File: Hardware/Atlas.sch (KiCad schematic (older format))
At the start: 46 parts, among them J1 DC, U1 MS5611, U2 HTU21D, U3 uSD Card, U4 RFD900, U5 MPU9150, U6 XBEE, U7 VENUS838LPX-L, U8 AOZ1031

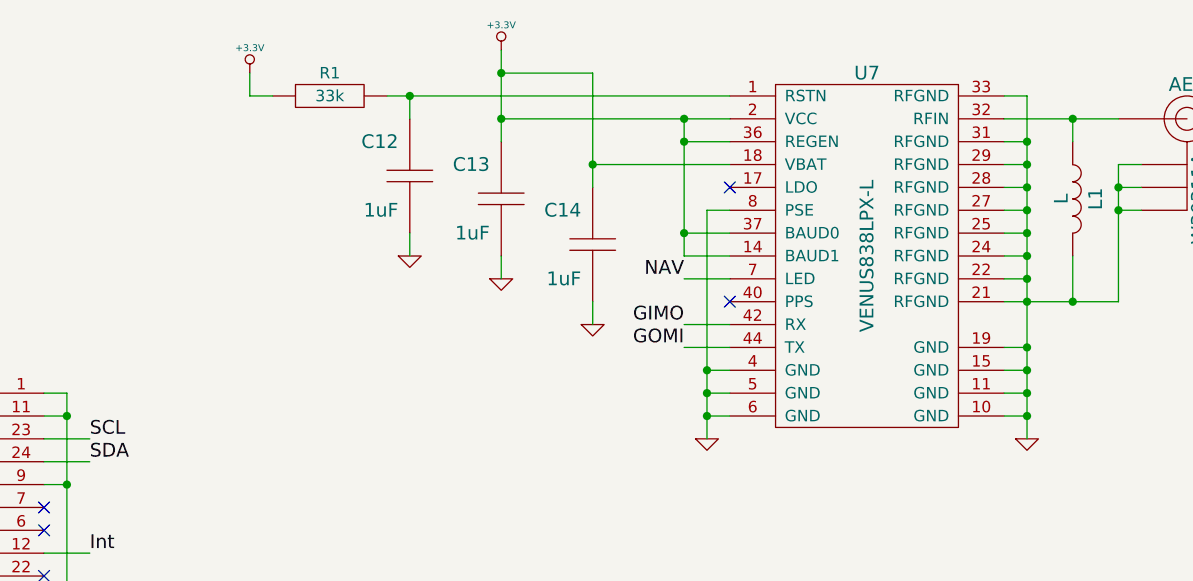
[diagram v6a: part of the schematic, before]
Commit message: Update GPS to support Flash and ROM versions
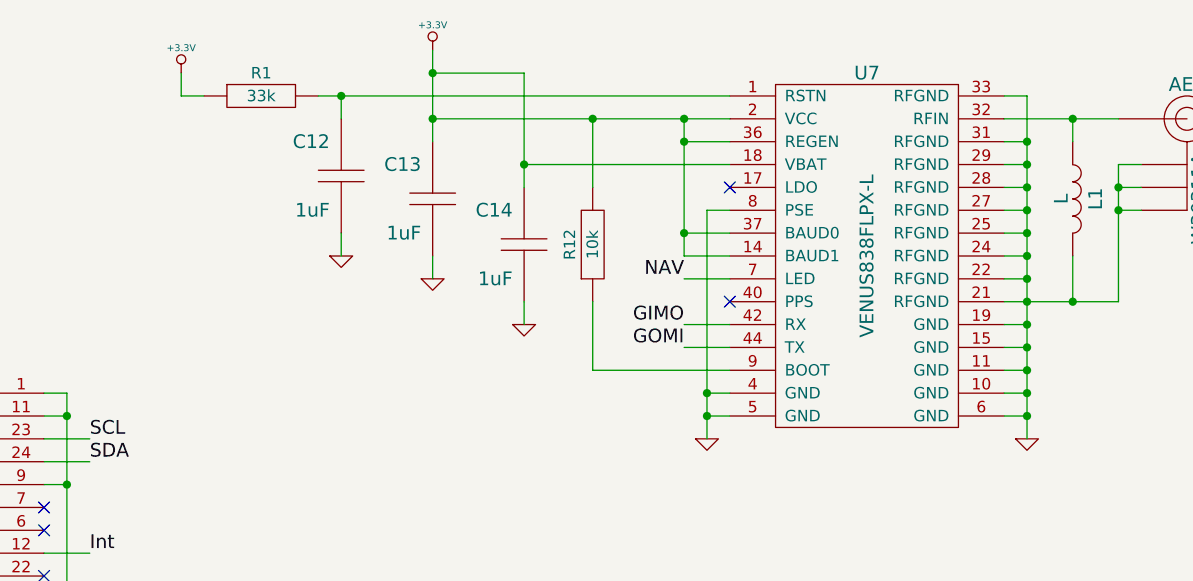
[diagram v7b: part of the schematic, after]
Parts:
- removed U7: VENUS838LPX-L, symbol VENUS838LPX-L
- added R12: 10k, RESC1608-N, symbol R
- added U7: VENUS838FLPX-L, ~, symbol VENUS838FLPX-L
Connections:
- net +3.3V: now also R12.2, U7.14 (BAUD1), U7.18 (VBAT), U7.2 (VCC), U7.36 (REGEN), U7.37 (BAUD0)
- net GIMO: now also U7.42 (RX)
- net GND: now also U7.10 (GND), U7.11 (GND), U7.15 (GND), U7.19 (GND), U7.21 (RFGND), U7.22 (RFGND), U7.24 (RFGND), U7.25 (RFGND), U7.27 (RFGND), U7.28 (RFGND), U7.29 (RFGND), U7.31 (RFGND), U7.33 (RFGND), U7.4 (GND), U7.5 (GND), U7.6 (GND), U7.8 (PSE)
- net GOMI: now also U7.44 (TX)
- net NAV: now also U7.7 (LED)
- net at C12.1, R1.2: now also U7.1 (RSTN)
- net at AE1.P, L1.2: now also U7.32 (RFIN)
- new net: R12.1, U7.9 (BOOT)
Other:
- moved on the sheet: C12, C13, C14, R1
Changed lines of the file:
@@
 Sheet 1 1
 Title "Atlas (Nucleo Shield)"
-Date "26 may 2014"
+Date "1 jun 2014"
 Rev "1"
 Comp "Aerodyne Labs"
@@
 L R R1
 U 1 1 537F99E2
-P 7050 1100
-F 0 "R1" H 7050 1200 50  0000 C CNN
-F 1 "33k" H 7050 1100 50  0000 C CNN
-F 2 "~" H 7050 1100 60  0000 C CNN
-F 3 "~" H 7050 1100 60  0000 C CNN
-F 4 "W" H 7050 1000 50  0001 C CNN "Power"
-F 5 "%" H 7050 900 50  0001 C CNN "Tolerance"
-	1    7050 1100
+P 6750 1100
+F 0 "R1" H 6750 1200 50  0000 C CNN
+F 1 "33k" H 6750 1100 50  0000 C CNN
+F 2 "~" H 6750 1100 60  0000 C CNN
+F 3 "~" H 6750 1100 60  0000 C CNN
+F 4 "W" H 6750 1000 50  0001 C CNN "Power"
+F 5 "%" H 6750 900 50  0001 C CNN "Tolerance"
+	1    6750 1100
 	1    0    0    -1
 $EndComp
@@
 L C C12
 U 1 1 537F99FD
-P 7400 1450
-F 0 "C12" H 7450 1600 60  0000 L CNN
-F 1 "1uF" H 7450 1300 60  0000 L CNN
-F 2 "CAPC1608-N" H 7400 1450 60  0001 C CNN
-F 3 "~" H 7400 1450 60  0000 C CNN
-F 4 "Samsung" H 7400 1450 60  0001 C CNN "MFR Name"
-F 5 "CL10B105KP8NNNC" H 7400 1450 60  0001 C CNN "MFR Part No"
-F 6 "1276-1946-1-ND" H 7400 1450 60  0001 C CNN "Distributor Part No"
-F 7 "10V" H 7350 1300 60  0001 R CNN "Voltage"
-F 8 "X7R" H 7350 1600 60  0001 R CNN "Dielectric"
-	1    7400 1450
+P 7100 1450
+F 0 "C12" H 7150 1600 60  0000 L CNN
+F 1 "1uF" H 7150 1300 60  0000 L CNN
+F 2 "CAPC1608-N" H 7100 1450 60  0001 C CNN
+F 3 "~" H 7100 1450 60  0000 C CNN
+F 4 "Samsung" H 7100 1450 60  0001 C CNN "MFR Name"
+F 5 "CL10B105KP8NNNC" H 7100 1450 60  0001 C CNN "MFR Part No"
+F 6 "1276-1946-1-ND" H 7100 1450 60  0001 C CNN "Distributor Part No"
+F 7 "10V" H 7050 1300 60  0001 R CNN "Voltage"
+F 8 "X7R" H 7050 1600 60  0001 R CNN "Dielectric"
+	1    7100 1450
 	-1   0    0    -1
 $EndComp
@@
 L +3.3V #PWR017
 U 1 1 537F9A2D
-P 6700 1000
-F 0 "#PWR017" H 6700 960 30  0001 C CNN
-F 1 "+3.3V" H 6700 1110 30  0000 C CNN
-F 2 "" H 6700 1000 60  0000 C CNN
-F 3 "" H 6700 1000 60  0000 C CNN
-	1    6700 1000
-	1    0    0    -1
-$EndComp
-$Comp
-L VENUS838LPX-L U7
-U 1 1 537FB717
-P 9400 1800
-F 0 "U7" H 9400 2600 60  0000 C CNN
-F 1 "VENUS838LPX-L" V 9400 1800 60  0000 C CNN
-F 2 "" H 9400 1800 60  0000 C CNN
-F 3 "" H 9400 1800 60  0000 C CNN
-	1    9400 1800
+P 6400 1000
+F 0 "#PWR017" H 6400 960 30  0001 C CNN
+F 1 "+3.3V" H 6400 1110 30  0000 C CNN
+F 2 "" H 6400 1000 60  0000 C CNN
+F 3 "" H 6400 1000 60  0000 C CNN
+	1    6400 1000
 	1    0    0    -1
 $EndComp
@@
 L +3.3V #PWR018
 U 1 1 537FB7C0
-P 7800 900
-F 0 "#PWR018" H 7800 860 30  0001 C CNN
-F 1 "+3.3V" H 7800 1010 30  0000 C CNN
-F 2 "" H 7800 900 60  0000 C CNN
-F 3 "" H 7800 900 60  0000 C CNN
-	1    7800 900
+P 7500 900
+F 0 "#PWR018" H 7500 860 30  0001 C CNN
+F 1 "+3.3V" H 7500 1010 30  0000 C CNN
+F 2 "" H 7500 900 60  0000 C CNN
+F 3 "" H 7500 900 60  0000 C CNN
+	1    7500 900
 	1    0    0    -1
 $EndComp
@@
 L GND #PWR020
 U 1 1 537FBC7D
-P 8200 2100
-F 0 "#PWR020" H 8200 2100 30  0001 C CNN
-F 1 "GND" H 8200 2030 30  0001 C CNN
-F 2 "" H 8200 2100 60  0000 C CNN
-F 3 "" H 8200 2100 60  0000 C CNN
-	1    8200 2100
+P 7900 2100
+F 0 "#PWR020" H 7900 2100 30  0001 C CNN
+F 1 "GND" H 7900 2030 30  0001 C CNN
+F 2 "" H 7900 2100 60  0000 C CNN
+F 3 "" H 7900 2100 60  0000 C CNN
+	1    7900 2100
 	1    0    0    -1
 $EndComp
@@
 L GND #PWR021
 U 1 1 537FBC8C
-P 7800 1900
-F 0 "#PWR021" H 7800 1900 30  0001 C CNN
-F 1 "GND" H 7800 1830 30  0001 C CNN
-F 2 "" H 7800 1900 60  0000 C CNN
-F 3 "" H 7800 1900 60  0000 C CNN
-	1    7800 1900
+P 7500 1900
+F 0 "#PWR021" H 7500 1900 30  0001 C CNN
+F 1 "GND" H 7500 1830 30  0001 C CNN
+F 2 "" H 7500 1900 60  0000 C CNN
+F 3 "" H 7500 1900 60  0000 C CNN
+	1    7500 1900
 	1    0    0    -1
 $EndComp
@@
 L GND #PWR022
 U 1 1 537FBD1D
-P 7400 1800
-F 0 "#PWR022" H 7400 1800 30  0001 C CNN
-F 1 "GND" H 7400 1730 30  0001 C CNN
-F 2 "" H 7400 1800 60  0000 C CNN
-F 3 "" H 7400 1800 60  0000 C CNN
-	1    7400 1800
+P 7100 1800
+F 0 "#PWR022" H 7100 1800 30  0001 C CNN
+F 1 "GND" H 7100 1730 30  0001 C CNN
+F 2 "" H 7100 1800 60  0000 C CNN
+F 3 "" H 7100 1800 60  0000 C CNN
+	1    7100 1800
 	1    0    0    -1
 $EndComp
@@
 L C C13
 U 1 1 537FD0BB
-P 7800 1550
-F 0 "C13" H 7850 1700 60  0000 L CNN
-F 1 "1uF" H 7850 1400 60  0000 L CNN
-F 2 "CAPC1608-N" H 7800 1550 60  0001 C CNN
-F 3 "~" H 7800 1550 60  0000 C CNN
-F 4 "Samsung" H 7800 1550 60  0001 C CNN "MFR Name"
-F 5 "CL10B105KP8NNNC" H 7800 1550 60  0001 C CNN "MFR Part No"
-F 6 "1276-1946-1-ND" H 7800 1550 60  0001 C CNN "Distributor Part No"
-F 7 "10V" H 7750 1400 60  0001 R CNN "Voltage"
-F 8 "X7R" H 7750 1700 60  0001 R CNN "Dielectric"
-	1    7800 1550
+P 7500 1550
+F 0 "C13" H 7550 1700 60  0000 L CNN
+F 1 "1uF" H 7550 1400 60  0000 L CNN
+F 2 "CAPC1608-N" H 7500 1550 60  0001 C CNN
+F 3 "~" H 7500 1550 60  0000 C CNN
+F 4 "Samsung" H 7500 1550 60  0001 C CNN "MFR Name"
+F 5 "CL10B105KP8NNNC" H 7500 1550 60  0001 C CNN "MFR Part No"
+F 6 "1276-1946-1-ND" H 7500 1550 60  0001 C CNN "Distributor Part No"
+F 7 "10V" H 7450 1400 60  0001 R CNN "Voltage"
+F 8 "X7R" H 7450 1700 60  0001 R CNN "Dielectric"
+	1    7500 1550
 	-1   0    0    -1
 $EndComp
@@
 L C C14
 U 1 1 537FD0C6
-P 8200 1750
-F 0 "C14" H 8250 1900 60  0000 L CNN
-F 1 "1uF" H 8250 1600 60  0000 L CNN
-F 2 "CAPC1608-N" H 8200 1750 60  0001 C CNN
-F 3 "~" H 8200 1750 60  0000 C CNN
-F 4 "Samsung" H 8200 1750 60  0001 C CNN "MFR Name"
-F 5 "CL10B105KP8NNNC" H 8200 1750 60  0001 C CNN "MFR Part No"
-F 6 "1276-1946-1-ND" H 8200 1750 60  0001 C CNN "Distributor Part No"
-F 7 "10V" H 8150 1600 60  0001 R CNN "Voltage"
-F 8 "X7R" H 8150 1900 60  0001 R CNN "Dielectric"
-	1    8200 1750
+P 7900 1750
+F 0 "C14" H 7950 1900 60  0000 L CNN
+F 1 "1uF" H 7950 1600 60  0000 L CNN
+F 2 "CAPC1608-N" H 7900 1750 60  0001 C CNN
+F 3 "~" H 7900 1750 60  0000 C CNN
+F 4 "Samsung" H 7900 1750 60  0001 C CNN "MFR Name"
+F 5 "CL10B105KP8NNNC" H 7900 1750 60  0001 C CNN "MFR Part No"
+F 6 "1276-1946-1-ND" H 7900 1750 60  0001 C CNN "Distributor Part No"
+F 7 "10V" H 7850 1600 60  0001 R CNN "Voltage"
+F 8 "X7R" H 7850 1900 60  0001 R CNN "Dielectric"
+	1    7900 1750
 	-1   0    0    -1
 $EndComp
@@
 	14400 5400 14400 5600
 Wire Wire Line
-	6700 1000 6700 1100
-Wire Wire Line
-	6700 1100 6800 1100
-Wire Wire Line
-	7300 1100 8800 1100
-Wire Wire Line
-	7400 1200 7400 1100
-Connection ~ 7400 1100
-Wire Wire Line
-	7800 900  7800 1300
-Wire Wire Line
-	7800 1200 8800 1200
-Connection ~ 7800 1200
+	6400 1000 6400 1100
+Wire Wire Line
+	6400 1100 6500 1100
+Wire Wire Line
+	7000 1100 8800 1100
+Wire Wire Line
+	7100 1200 7100 1100
+Connection ~ 7100 1100
+Wire Wire Line
+	7500 900  7500 1300
+Wire Wire Line
+	7500 1200 8800 1200
+Connection ~ 7500 1200
 Wire Wire Line
 	8800 1300 8600 1300
@@
 	8800 2400 8700 2400
 Connection ~ 8700 2500
-Wire Wire Line
-	8800 2300 8700 2300
 Connection ~ 8700 2400
 Wire Wire Line
-	7800 1000 8200 1000
-Wire Wire Line
-	8200 1000 8200 1500
-Connection ~ 7800 1000
-Wire Wire Line
-	8800 1400 8200 1400
-Connection ~ 8200 1400
-Wire Wire Line
-	7400 1800 7400 1700
-Wire Wire Line
-	7800 1800 7800 1900
-Wire Wire Line
-	8200 2000 8200 2100
+	7500 1000 7900 1000
+Wire Wire Line
+	7900 1000 7900 1500
+Connection ~ 7500 1000
+Wire Wire Line
+	8800 1400 7900 1400
+Connection ~ 7900 1400
+Wire Wire Line
+	7100 1800 7100 1700
+Wire Wire Line
+	7500 1800 7500 1900
+Wire Wire Line
+	7900 2000 7900 2100
 Wire Wire Line
 	8800 1600 8700 1600
-Connection ~ 8700 2300
 Wire Wire Line
 	8600 1900 8800 1900
@@
 Wire Wire Line
 	10900 8600 11000 8600
+$Comp
+L VENUS838FLPX-L U7
+U 1 1 538B8B92
+P 9400 1800
+F 0 "U7" H 9400 2600 60  0000 C CNN
+F 1 "VENUS838FLPX-L" V 9400 1800 60  0000 C CNN
+F 2 "~" H 9400 1800 60  0000 C CNN
+F 3 "~" H 9400 1800 60  0000 C CNN
+	1    9400 1800
+	1    0    0    -1
+$EndComp
+Wire Wire Line
+	10000 2100 10100 2100
+Connection ~ 10100 2100
+Wire Wire Line
+	8200 2000 8200 2300
+Wire Wire Line
+	8200 2300 8800 2300
+Wire Wire Line
+	8200 1500 8200 1200
+Connection ~ 8200 1200
+$Comp
+L R R12
+U 1 1 538B8FA4
+P 8200 1750
+F 0 "R12" H 8200 1850 50  0000 C CNN
+F 1 "10k" H 8200 1750 50  0000 C CNN
+F 2 "RESC1608-N" H 8200 1750 60  0001 C CNN
+F 3 "~" H 8200 1750 60  0000 C CNN
+F 4 "Rohm" H 8200 1750 60  0001 C CNN "MFR Name"
+F 5 "MCR03ERTJ103" H 8200 1750 60  0001 C CNN "MFR Part No"
+F 6 "RHM10KCGCT-ND" H 8200 1750 60  0001 C CNN "Distributor Part No"
+F 7 "1/10W" H 8200 1650 50  0001 C CNN "Power"
+F 8 "5%" H 8200 1550 50  0001 C CNN "Tolerance"
+	1    8200 1750
+	0    -1   -1   0
+$EndComp
 $EndSCHEMATC
